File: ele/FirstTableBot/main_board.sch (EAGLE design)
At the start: 107 parts, among them IC1 MCP602ST, X4 POWER_IN

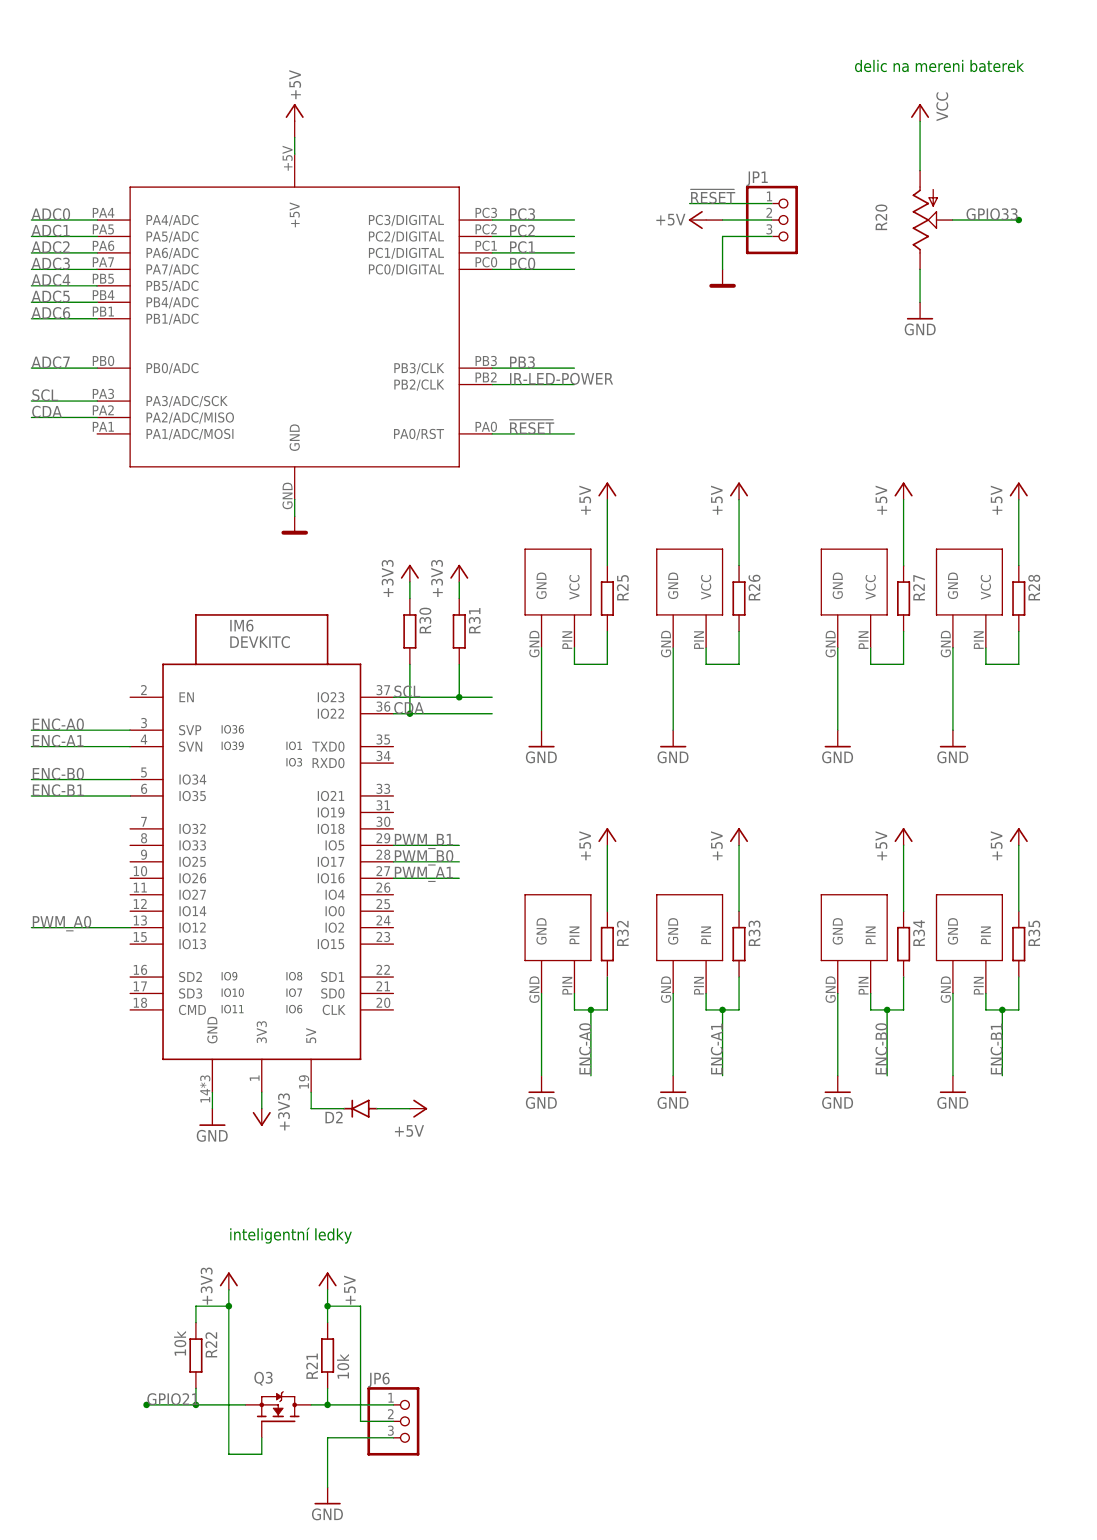
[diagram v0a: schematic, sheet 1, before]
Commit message: serialiyovani ir-led encoderu a zpetivoltovac I2C
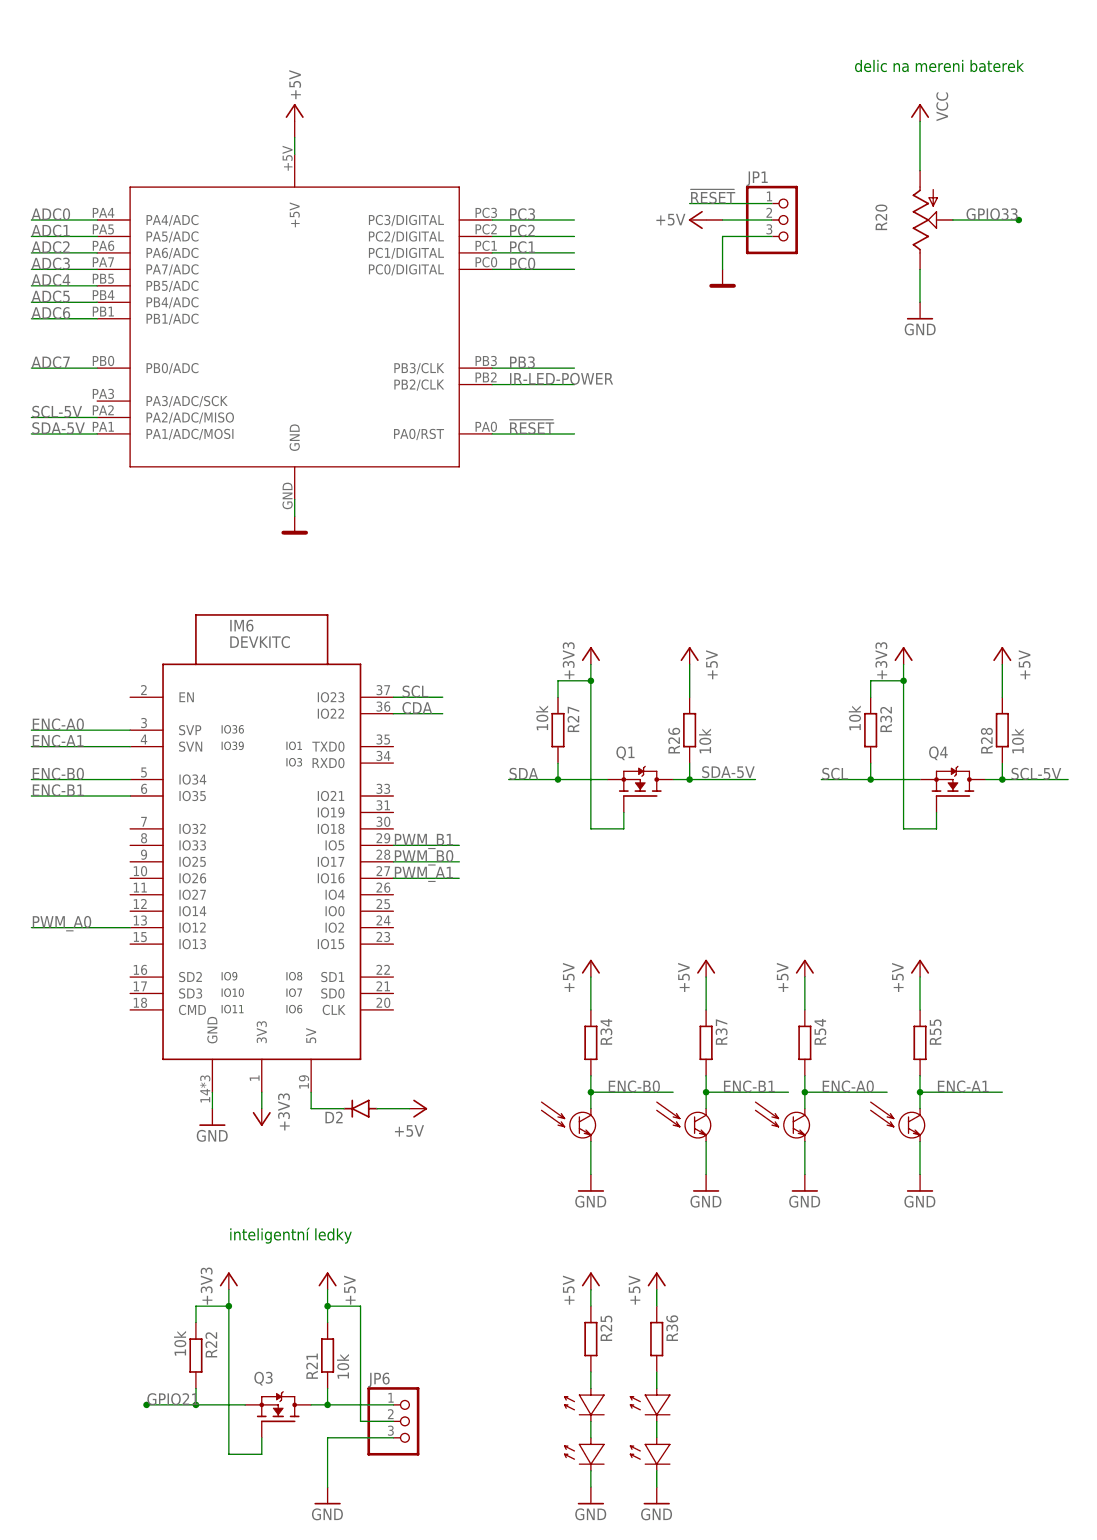
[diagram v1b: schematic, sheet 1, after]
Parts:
- removed R30, R31, R33, R35: (no value), resistor:R-EU_R0603
- removed U$10, U$12, U$14: L-NP-3C1, led-brt:L-NP-3C1
- removed U$17, U$18, U$19: BIR-NM13C1, led-brt:BIR-NM13C1
- added Q1, Q4: (no value), transistors:N-MOSFET-SOT23-DIST
- added R36, R37, R54, R55: (no value), resistor:R-EU_R0603
- added U$11, U$15, U$20: BIR-NM13C1, led-brt:BIR-NM13C1
- added U$21, U$22, U$23: L-NP-3C1, led-brt:L-NP-3C1
- R26, R27, R28, R32: value (none) -> 10k; device resistor:R-EU_R0603 -> resistor:R-EU_R0402
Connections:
- removed net N$18: R26.2, U$17.VCC
- removed net N$19: R27.2, U$18.VCC
- removed net N$20: R28.2, U$19.VCC
- new net N$21: U$11.VCC, U$16.GND
- new net N$22: R36.2, U$15.VCC
- new net N$31: U$15.GND, U$20.VCC
- new net SCL-5V: Q4.D, R28.1, U$8.PA2/ADC/MISO
- new net SDA: Q1.S, R27.2
- new net SDA-5V: Q1.D, R26.1, U$8.PA1/ADC/MOSI
- net +3V3: now also Q1.G, Q4.G, R27.1, R32.1; no longer R30.1, R31.1
- net +5V: now also R26.2, R28.2, R36.1, R37.1, R54.1, R55.1; no longer R26.1, R27.1, R28.1, R32.1, R33.1, R35.1
- net CDA: no longer R30.2, U$8.PA2/ADC/MISO
- net ENC-A0: now also R54.2, U$22.PIN; no longer R32.2, U$10.PIN
- net ENC-A1: now also R55.2, U$23.PIN; no longer R33.2, U$12.PIN
- net ENC-B1: now also R37.2, U$21.PIN; no longer R35.2, U$14.PIN
- net GND: now also U$11.GND, U$20.GND, U$21.GND, U$22.GND, U$23.GND; no longer U$10.GND, U$12.GND, U$14.GND, U$16.GND, U$17.GND, U$18.GND, U$19.GND
- net SCL: now also Q4.S, R32.2; no longer R31.2, U$8.PA3/ADC/SCK
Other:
- moved on the sheet: R25, R26, R27, R28, R32, R34

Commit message: dolni propust k zesilovacum
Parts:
- added C10, C11, C12, C13: (no value), resistor:C-EUC1206
- added R30, R31, R33, R35: (no value), resistor:R-EU_R0603
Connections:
- removed net N$29: IC1A.-IN, R51.2, R53.1
- new net N$18: C11.1, R30.2, R31.1
- new net N$19: C10.1, IC1B.+IN, R30.1
- new net N$20: IC1A.-IN, R33.2, R35.1
- new net N$32: C13.1, R51.2, R53.1
- new net N$33: C12.1, IC1A.+IN, R51.1
- net +3V3: now also IC1P.V+
- net AMPLIFIED_I-MOT_A: now also C13.2, R35.2; no longer R53.2
- net AMPLIFIED_I-MOT_B: now also C11.2
- net GND: now also C10.2, C12.2, R33.1; no longer R51.1
- net I-MOT_A: now also R53.2; no longer IC1A.+IN
- net I-MOT_B: now also R31.2; no longer IC1B.+IN
- net VCC: no longer IC1P.V+
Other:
- moved on the sheet: IC1A, IC1B, R50, R51, R52, R53

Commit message: napajeni IR-led senzoru
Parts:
- removed R13, R3, R7: (no value), resistor:R-EU_R0603
- added Q8: (no value), transistors:P-MOSFET-MLP_HS
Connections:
- removed net N$7: R13.2, U$7.A
- new net N$29: U$6.C, U$7.A
- new net N$34: Q8.S, R1.1, R11.1, R5.1, R9.1
- net +5V: now also Q8.D
- net GND: no longer U$2.C, U$3.C, U$6.C
- net IR-LED-POWER: now also Q8.G; no longer R1.1, R11.1, R13.1, R3.1, R5.1, R7.1, R9.1
- net N$2: now also U$2.C; no longer R3.2
- net N$4: now also U$3.C; no longer R7.2
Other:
- moved on the sheet: C1, C10, C11, C12, C13, C2, C23, C6, C7, D3, IC1A, IC1B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

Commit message: piniste
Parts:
- added JP2, JP7, JP8: (no value), pinhead:PINHD-2X13
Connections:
- removed net GPIO21: Q3.S, R22.2
- removed net GPIO33: R20.S
- new net BAT-REF: IM6.IO33, R20.S
- new net I-LED: IM6.IO21, Q3.S, R22.2
- new net IO13: IM6.IO13, JP2.19, JP2.20
- new net IO14: IM6.IO14, JP2.17, JP2.18
- new net IO16: IM6.IO16, JP2.15, JP2.16
- new net IO17: IM6.IO17, JP2.13, JP2.14
- new net IO18: IM6.IO18, JP2.11, JP2.12
- new net IO19: IM6.IO19, JP2.10, JP2.9
- new net IO25: IM6.IO25, JP2.7, JP2.8
- new net IO26: IM6.IO26, JP2.5, JP2.6
- new net IO27: IM6.IO27, JP2.3, JP2.4
- new net IO32: IM6.IO32, JP2.1, JP2.2
- new net IO4: IM6.IO4, JP2.21, JP2.22
- new net RX: IM6.RXD0, JP2.25, JP2.26
- new net TX: IM6.TXD0, JP2.23, JP2.24
- net +3V3: now also JP7.10, JP7.12, JP7.14, JP7.16, JP7.18, JP7.2, JP7.20, JP7.22, JP7.24, JP7.26, JP7.4, JP7.6, JP7.8, JP8.10, JP8.12, JP8.14, JP8.16, JP8.18, JP8.2, JP8.20, JP8.22, JP8.24, JP8.26, JP8.4, JP8.6, JP8.8, R34.1, R37.1, R54.1, R55.1
- net +5V: no longer R34.1, R37.1, R54.1, R55.1
- net GND: now also JP7.1, JP7.11, JP7.13, JP7.15, JP7.17, JP7.19, JP7.21, JP7.23, JP7.25, JP7.3, JP7.5, JP7.7, JP7.9, JP8.1, JP8.11, JP8.13, JP8.15, JP8.17, JP8.19, JP8.21, JP8.23, JP8.25, JP8.3, JP8.5, JP8.7, JP8.9
- net PWM_A1: now also IM6.IO15; no longer IM6.IO16
- net PWM_B0: now also IM6.IO0; no longer IM6.IO17
- net SLEEP: now also IM6.IO2
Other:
- note added: "THIS SIGNAL MUST BE HERE!"

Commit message: zesilovace
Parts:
- R33, R50: value (none) -> 100
- R35, R52: value (none) -> 10k
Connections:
- removed net SW5: C3.2, JP4.8, R39.2, SW1.P, SW1.P1
- new net SW1: C3.2, JP4.7, R39.2, SW1.P, SW1.P1
- net GND: now also JP4.10, JP4.2, JP4.4, JP4.6, JP4.8; no longer JP4.1, JP4.3, JP4.5, JP4.7, JP4.9
- net SW0: now also JP4.9; no longer JP4.10
- net SW2: now also JP4.5; no longer JP4.6
- net SW3: now also JP4.3; no longer C8.2, JP4.4, R45.2, SW3.P, SW3.P1
- net SW4: now also C8.2, JP4.1, R45.2, SW3.P, SW3.P1; no longer JP4.2
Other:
- moved on the sheet: JP2, JP6, JP7, JP8, Q3, R21, R22

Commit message: napájení z powerbanki
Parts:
- added K1: ARK550/2, #PaJa_konektory:ARK550/2
- added Q7: (no value), transistors:P-MOSFET-MLP_HS
- added Q9: (no value), transistors:N-MOSFET-SOT23-GSD
- added R3: 2M, rcl_upravena:R-EU_R0805
- added R7: 100k, rcl_upravena:R-EU_R0805
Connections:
- new net N$35: Q7.G, Q9.G, R7.2
- new net N$7: Q2.D, Q9.S, R3.1, R7.1
- net +5V: now also JP3.2, JP5.2, K1.K2, Q7.D
- net GND: now also K1.K1, R3.2
- net VCC: now also Q7.S, Q9.D; no longer JP3.2, JP5.2, Q2.D
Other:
- moved on the sheet: C2, IM3, Q6, R15, R16, SW5

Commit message: nastrel_textu
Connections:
- net N$7: now also Q9.D; no longer Q9.S
- net VCC: now also Q9.S; no longer Q9.D
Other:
- moved on the sheet: Q7, Q9, R15, R16, R3, R7

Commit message: eagle_librarys
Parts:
- added Q10: (no value), transistors:N-MOSFET-SOT23-GSD
- added R13: (no value), resistor:R-EU_R0603
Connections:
- new net N$36: Q10.D, Q8.G, R13.1
- net +5V: now also R13.2
- net GND: now also Q10.S
- net IR-LED-POWER: now also Q10.G; no longer Q8.G
